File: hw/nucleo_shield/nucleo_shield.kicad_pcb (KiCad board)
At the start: 2 copper layers, 150.1 x 90.2 mm, 61 parts, among them CN101 Nucleo-F411RE-CN10, CN71 Nucleo-F411RE-CN7, P1 CONN_INH1, P10 CONN_OUTH1, P11 CONN_OUTH2, P12 CONN_RS485_OUT, P13 CONN_RS485_IN, P2 CONN_OUT3, P4 POWER_CON, P5 CONN_INH2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

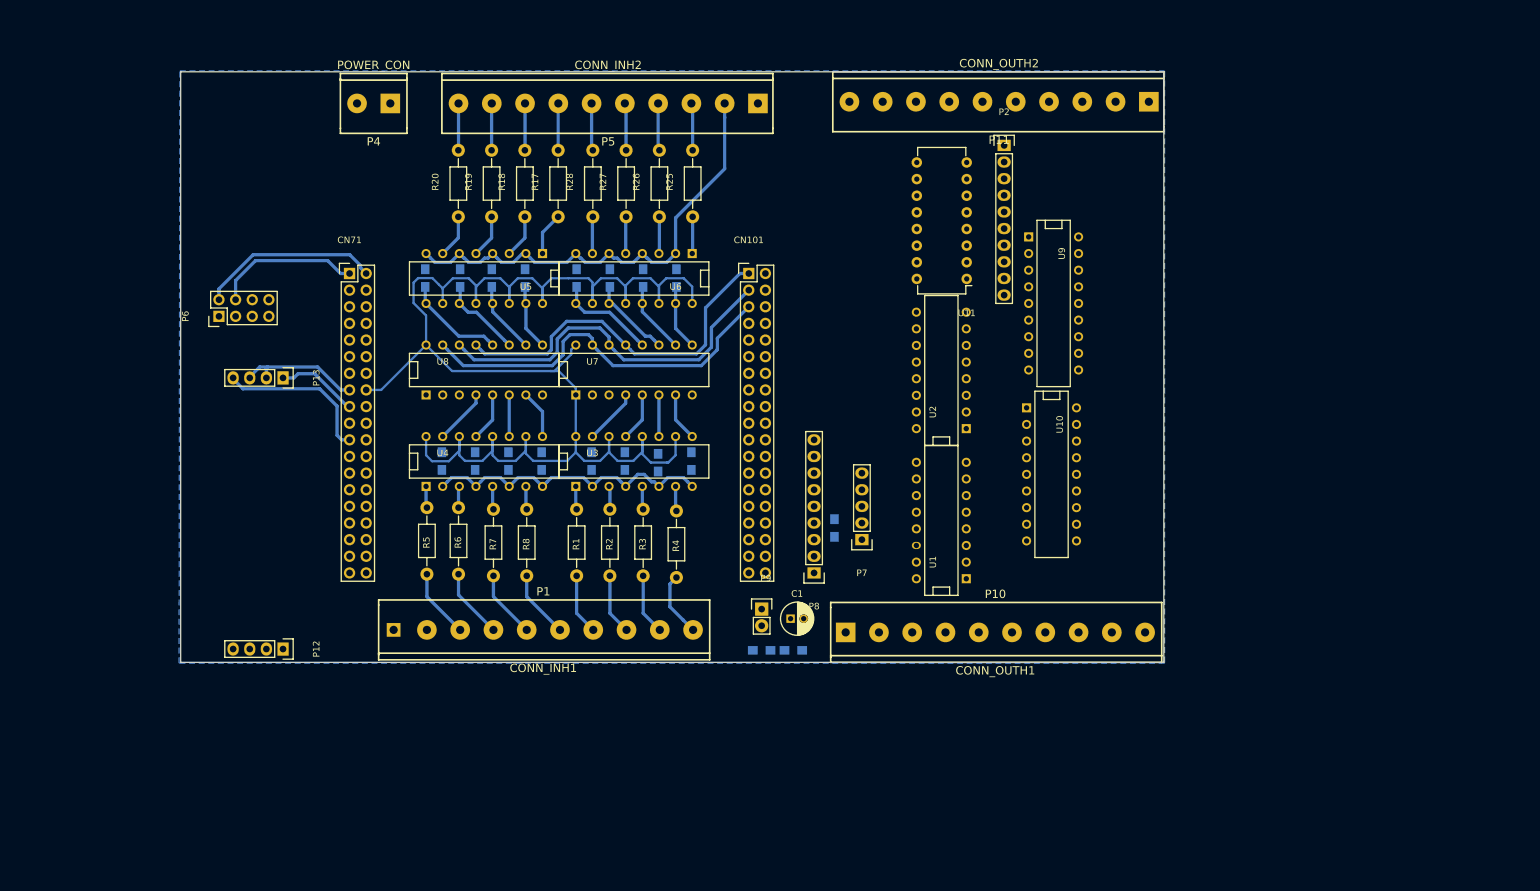
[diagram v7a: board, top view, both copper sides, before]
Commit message: Nucleo: add jumpers and outputs
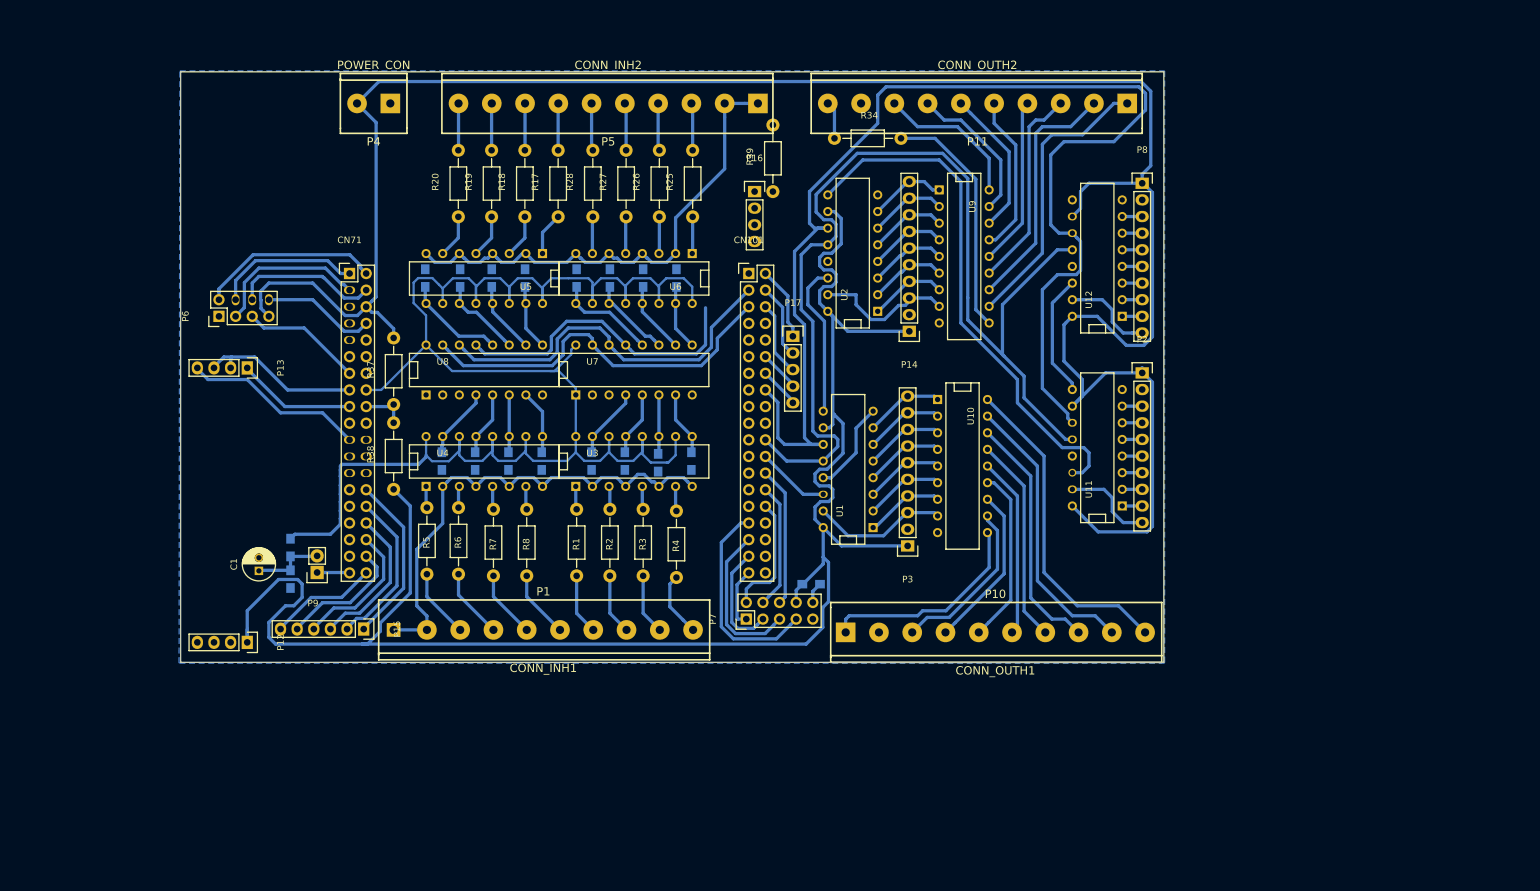
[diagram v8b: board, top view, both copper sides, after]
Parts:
- added P14: CONN_OUT2, Pin_Headers:Pin_Header_Straight_1x10, F.Cu at (206.8, 98.0)
- added P15: CONN_ANALOG, Pin_Headers:Pin_Header_Straight_1x06, F.Cu at (123.4, 143.5)
- added P16: CONN_EXTI2C, Pin_Headers:Pin_Header_Straight_1x04, F.Cu at (183.1, 76.7)
- added P17: CONN_EXT, Pin_Headers:Pin_Header_Straight_1x05, F.Cu at (189.0, 98.8)
- added P3: CONN_OUT1, Pin_Headers:Pin_Header_Straight_1x10, F.Cu at (206.5, 130.8)
- added R34: R, Resistors_ThroughHole:Resistor_Horizontal_RM10mm, F.Cu at (200.4, 68.6)
- added R37: R, Resistors_ThroughHole:Resistor_Horizontal_RM10mm, F.Cu at (128.0, 104.1)
- added R38: R, Resistors_ThroughHole:Resistor_Horizontal_RM10mm, F.Cu at (128.0, 117.1)
- added R39: R, Resistors_ThroughHole:Resistor_Horizontal_RM10mm, F.Cu at (185.9, 71.6)
- added U12: 74HC595, Housings_DIP:DIP-16__300, F.Cu at (235.5, 86.9)
- P7: value SD_CONN -> CONN_LCD_SD; footprint Pin_Headers:Pin_Header_Straight_1x05 -> Pin_Headers:Pin_Header_Straight_2x05
- P8: value LCD_CONN -> CONN_OUT4; footprint Pin_Headers:Pin_Header_Straight_1x09 -> Pin_Headers:Pin_Header_Straight_1x10
- U11: footprint Housings_DIP:DIP-16_W7.62mm -> Housings_DIP:DIP-16__300
- moved C1 81.5 mm to (107.4, 134.6), turned to 90 degrees
- moved P8 77.8 mm to (242.3, 75.4), turned to 0 degrees
- moved R36 77.5 mm to (112.3, 135.9), turned to 270 degrees
- moved R35 73.6 mm to (112.3, 131.1), turned to 270 degrees
- moved P9 68.1 mm to (116.3, 134.9), turned to 180 degrees
- moved P2 40.6 mm to (242.3, 104.4)
- moved U11 32.6 mm to (235.5, 115.8), turned to 90 degrees
- moved U2 22.4 mm to (198.1, 86.1)
- moved P7 21.4 mm to (181.9, 142.0), turned to 90 degrees
- moved U1 16.2 mm to (197.4, 119.1)
- moved U9 15.4 mm to (215.1, 86.6)
- moved U10 13.6 mm to (214.9, 118.6)
- moved R33 9.28 mm to (191.8, 136.7), turned to 0 degrees
- moved P13 5.67 mm to (105.7, 103.6)
- moved P12 5.55 mm to (105.7, 145.5)
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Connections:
- CN101 pad 12: SRCLK -> Net-(CN101-Pad12)
- CN101 pad 14: SRLatch -> Net-(CN101-Pad14)
- CN101 pad 16: SRDATA -> SRCLK
- CN101 pad 2: SD_CS -> Net-(CN101-Pad2)
- CN101 pad 22: (no net) -> SRLatch
- CN101 pad 24: (no net) -> SRDATA
- CN101 pad 31: (no net) -> SD_CS
- CN101 pad 33: LCD_CS -> LCD_DC
- CN101 pad 34: SCT_IN -> (no net)
- CN101 pad 37: LCD_DC -> LCD_CS
- CN101 pad 4: (no net) -> Net-(CN101-Pad4)
- CN101 pad 6: (no net) -> Net-(CN101-Pad6)
- CN71 pad 28: (no net) -> Net-(CN71-Pad28)
- CN71 pad 30: (no net) -> Net-(CN71-Pad30)
- CN71 pad 32: (no net) -> Net-(CN71-Pad32)
- CN71 pad 34: (no net) -> Net-(CN71-Pad34)
- CN71 pad 36: (no net) -> Net-(CN71-Pad36)
- CN71 pad 37: (no net) -> SCT_IN
- CN71 pad 38: (no net) -> Net-(CN71-Pad38)
- P7 pad 1: SD_CS -> LCD_CS
- P7 pad 2: SPI1_MOSI -> SPI1_SCK
- P7 pad 3: SPI1_MISO -> LCD_RST
- P7 pad 4: SPI1_SCK -> SPI1_MISO
- P7 pad 5: (no net) -> LCD_DC
- P8 pad 3: LCD_CS -> out32
- P8 pad 4: LCD_RST -> out31
- P8 pad 5: LCD_DC -> out30
- P8 pad 6: SPI1_MOSI -> out29
- P8 pad 7: SPI1_SCK -> out28
- P8 pad 8: Net-(P8-Pad8) -> out27
- P8 pad 9: SPI1_MISO -> out26
- R33 pad 2: Net-(P8-Pad8) -> Net-(P7-Pad10)
- U11 pad 9: (no net) -> Net-(U11-Pad9)
- U9 pad 10: +24V -> Net-(R34-Pad2)
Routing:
- net +5V: track 0.00 -> 591.6 mm
- net SRCLK: track 0.00 -> 193.0 mm
- net SRLatch: track 0.00 -> 157.7 mm
- net Net-(U11-Pad14): track 0.00 -> 80.3 mm
- net out8h: track 0.00 -> 49.2 mm
- net out9h: track 0.00 -> 43.7 mm
- net out7h: track 0.00 -> 42.9 mm
- net +24V: track 0.00 -> 39.1 mm
- net out10h: track 0.00 -> 37.6 mm
- net out6h: track 0.00 -> 37.4 mm
- net Net-(R34-Pad2): track 0.00 -> 36.8 mm
- net GND_24V: track 118.3 -> 152.6 mm
- net GND: track 0.00 -> 31.9 mm
- net SD_CS: track 0.00 -> 31.7 mm
- net out5h: track 0.00 -> 31.6 mm
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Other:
- net class Default: clearance 0.4 -> 0.3; via_drill 1 -> 0.6
- net class mini removed
- rule trace_clearance: 0.4 -> 0.3
